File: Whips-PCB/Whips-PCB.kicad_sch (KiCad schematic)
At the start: 23 parts, among them J1 12 VDC, J2 RS422 BUS, J3 SPEAKER 4OHM, J4 TO WHIP, SW2 SW_DIP_x06, U2 MAX485ESA+T, U3 SN74AHCT125DR, U4 TSR_1-2450, U5 MAX98357AEWL_T, U6 Teensy4.1_Minimal

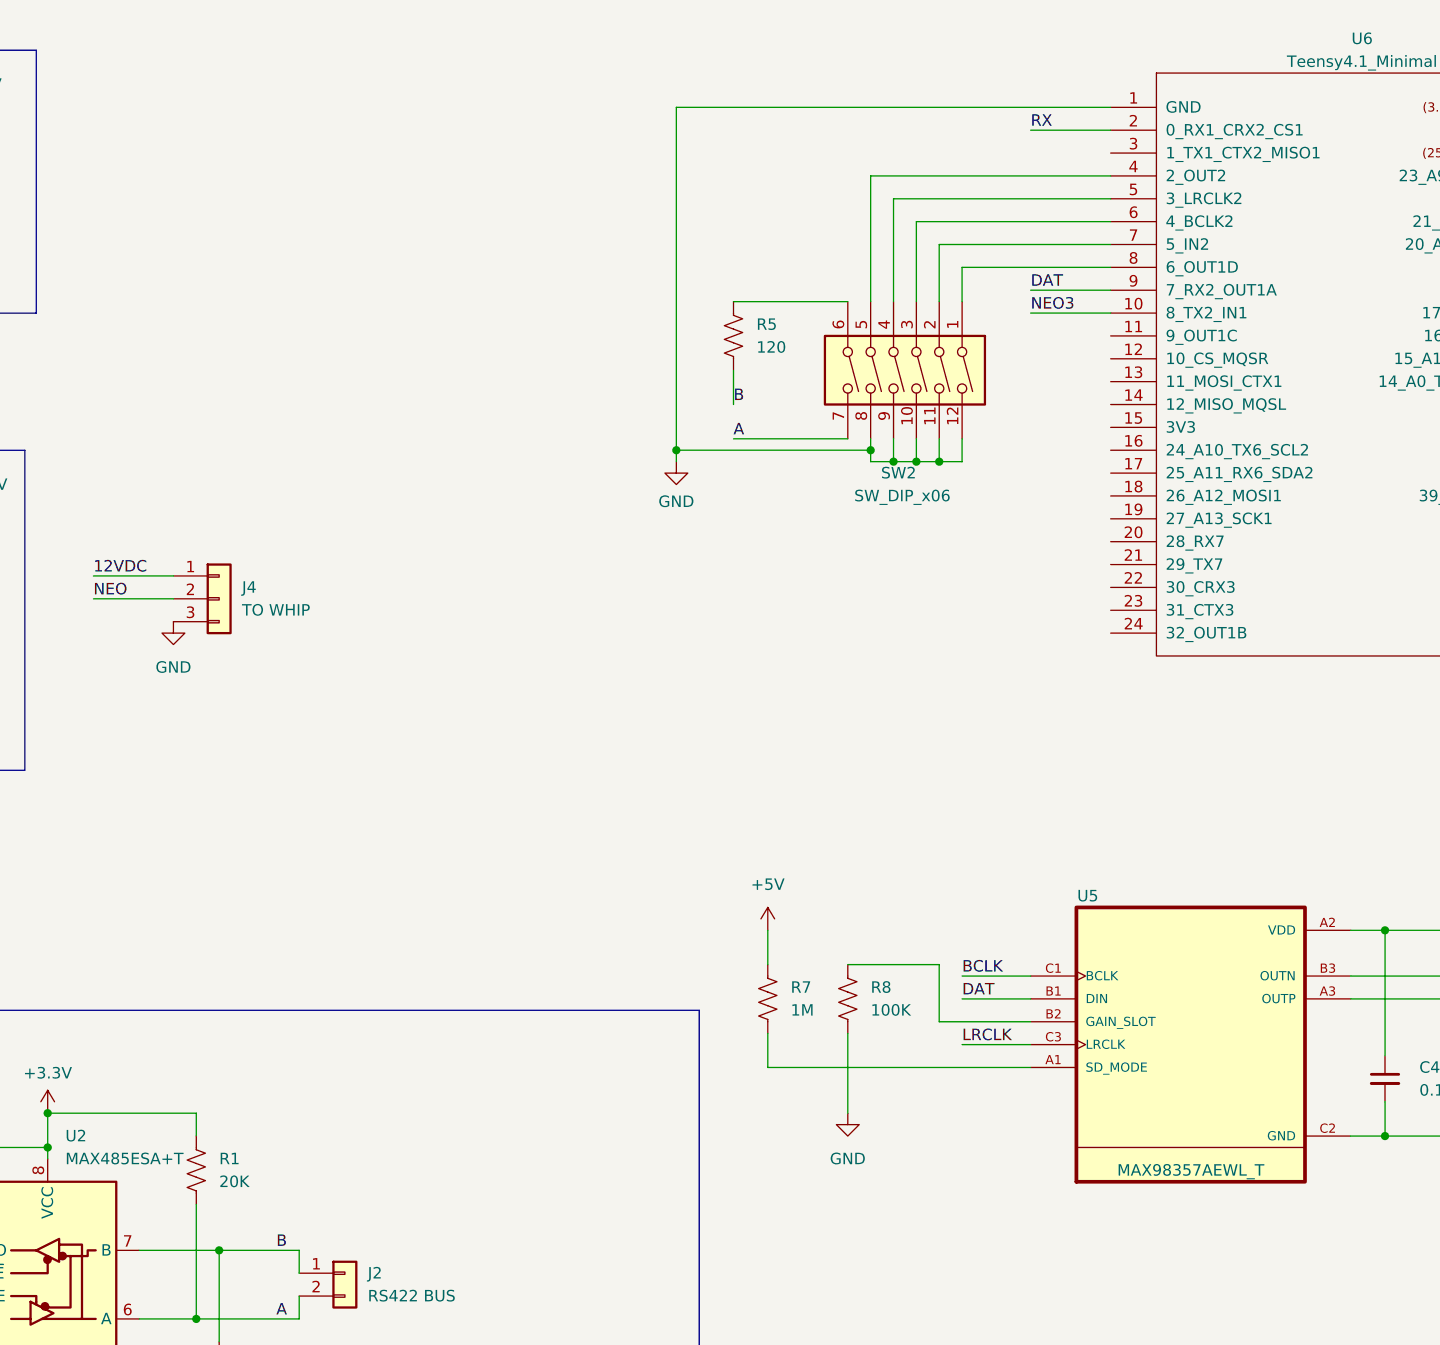
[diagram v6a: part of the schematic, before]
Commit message: support for indicator LEDS
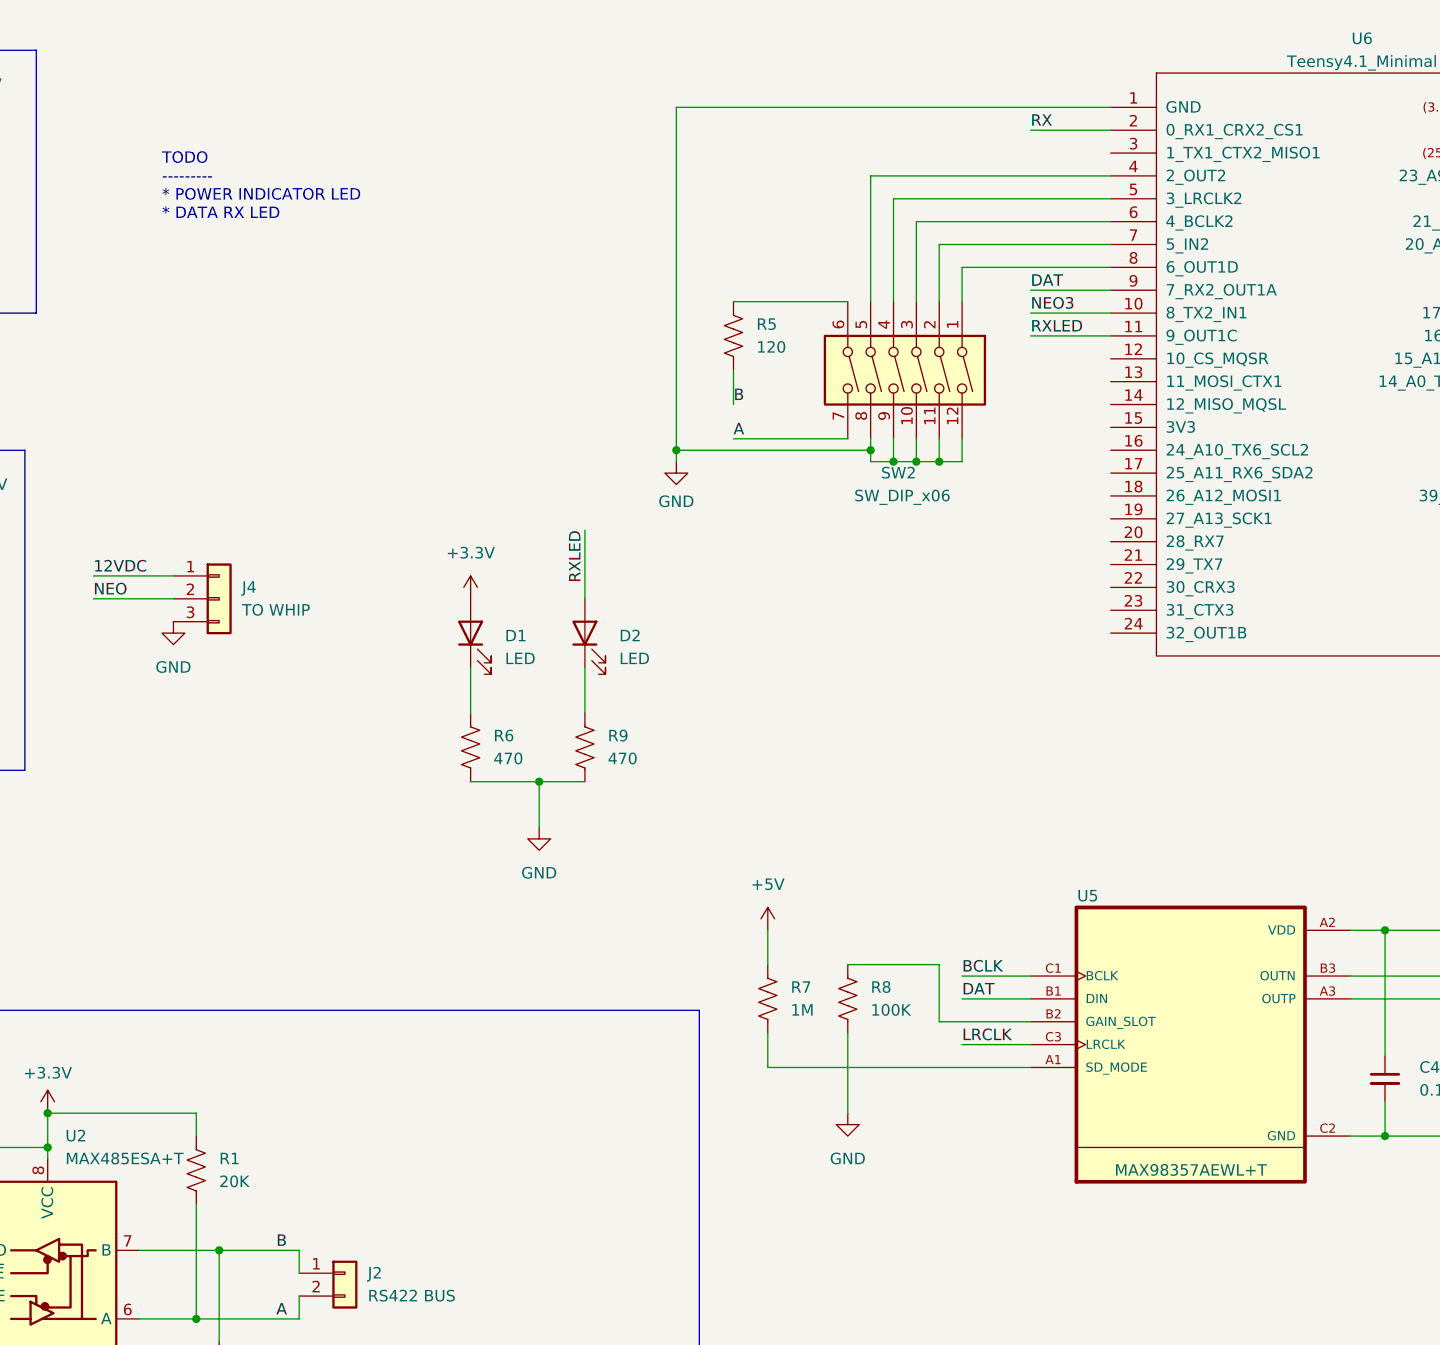
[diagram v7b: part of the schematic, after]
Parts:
- added D1, D2: LED, symbol Device:LED
- added R6, R9: 470, symbol Device:R_US
- C1, C4: footprint Capacitor_SMD:C_0201_0603Metric -> Capacitor_SMD:C_0402_1005Metric; LCSC C76934 -> C1525
- C2, C5: footprint Capacitor_SMD:C_0603_1608Metric -> Capacitor_SMD:C_0402_1005Metric; LCSC C1691 -> C15525
- J1, J2, J3: footprint (none) -> TerminalBlock_RND:TerminalBlock_RND_205-00001_1x02_P5.00mm_Horizontal; LCSC (none) -> C8404
- J4: footprint (none) -> TerminalBlock_RND:TerminalBlock_RND_205-00002_1x03_P5.00mm_Horizontal; LCSC (none) -> C8401
- R8: footprint Resistor_SMD:R_0805_2012Metric -> Resistor_SMD:R_0402_1005Metric; LCSC C149504 -> C25741
- SW2: footprint (none) -> Button_Switch_THT:SW_DIP_SPSTx06_Slide_6.7x16.8mm_W7.62mm_P2.54mm_LowProfile; LCSC C5160843 -> C2859410
- U2: footprint Package_SO:SOIC-8-1EP_3.9x4.9mm_P1.27mm_EP2.29x3mm -> Package_SO:SOIC-8_3.9x4.9mm_P1.27mm
- U4: LCSC (none) -> DNP
- U5: value MAX98357AEWL_T -> MAX98357AEWL+T; footprint MAX98357AEWL_T:BGA9N40P3X3_134X143X69N -> Package_BGA:WLP-9_1.448x1.468mm_Layout3x3_P0.4mm_Ball0.27mm_Pad0.25mm; LCSC (none) -> C2682619
- U6: footprint (none) -> teensy:Teensy41; LCSC (none) -> DNP
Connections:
- net +3.3V: now also D1.2 (A)
- net GND: now also R6.2, R9.2
- net RXLED: now reaches U6.11 (9_OUT1C)
- net RXLED: now also D2.2 (A)
- new net: D1.1 (K), R6.1
- new net: D2.1 (K), R9.1
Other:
- note added: "TODO --------- * POWER INDICATOR LED * DATA RX LED"

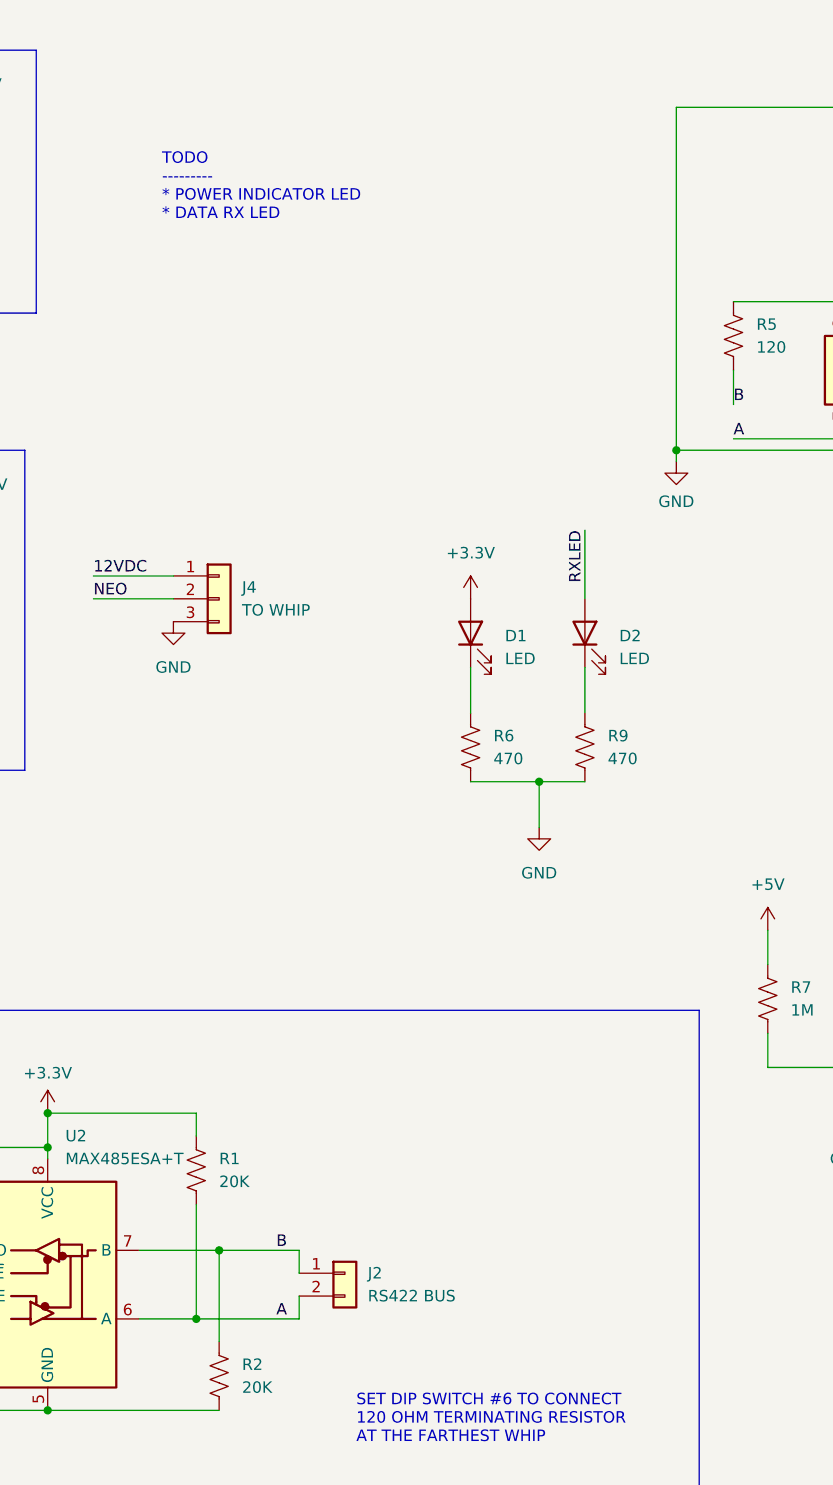
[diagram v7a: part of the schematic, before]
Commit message: provided parts and footprints for LEDs
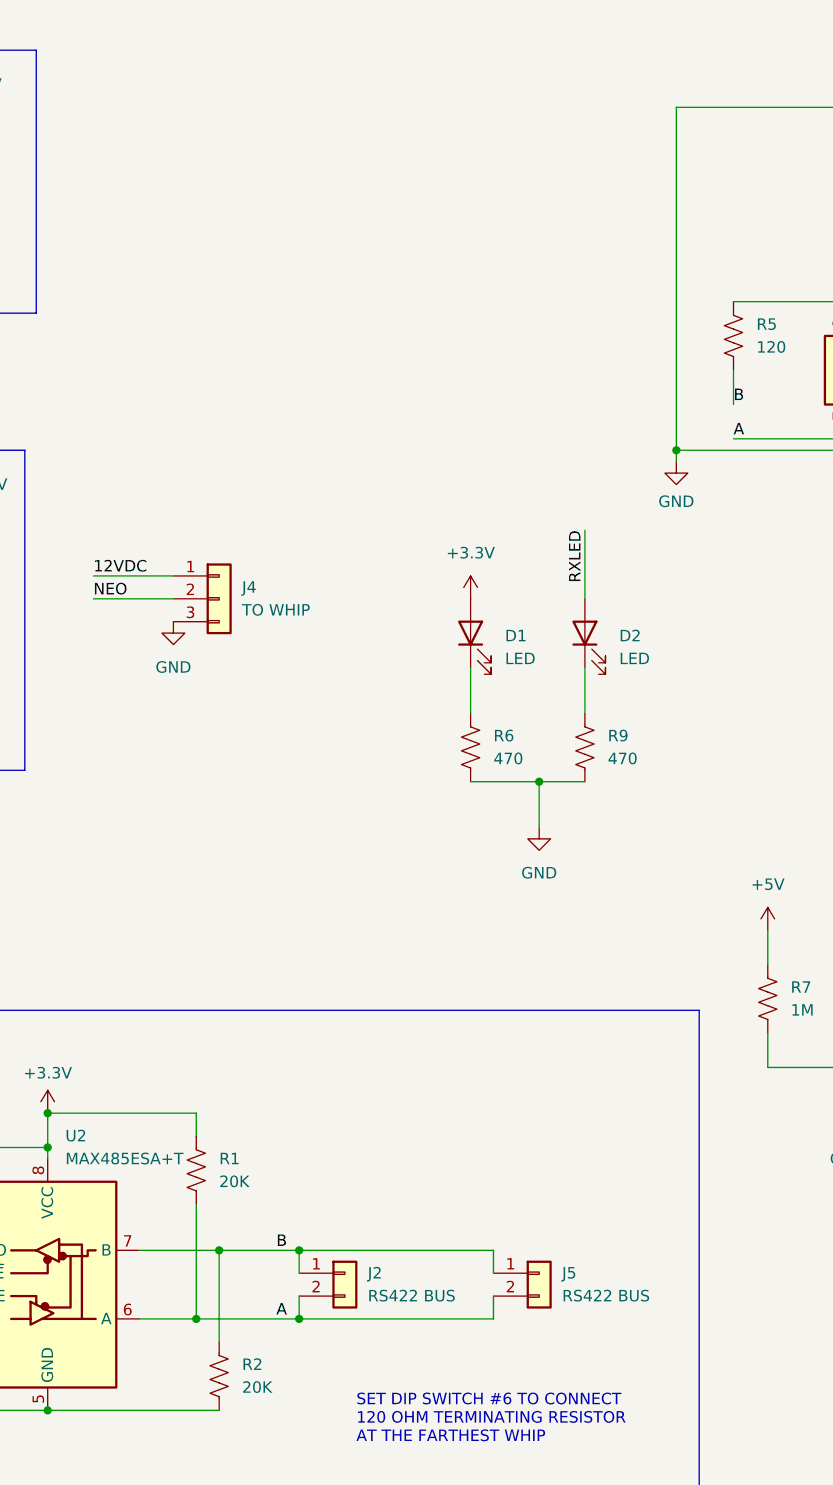
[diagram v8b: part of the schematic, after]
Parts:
- added J5: RS422 BUS, TerminalBlock_RND:TerminalBlock_RND_205-00001_1x02_P5.00mm_Horizontal, symbol Connector_Generic:Conn_01x02
- D1: footprint (none) -> LED_SMD:LED_0603_1608Metric; LCSC (none) -> C2286
- D2: footprint (none) -> LED_SMD:LED_0603_1608Metric; LCSC (none) -> C2290
- R6, R9: footprint (none) -> Resistor_SMD:R_0402_1005Metric; LCSC (none) -> C25117
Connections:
- net A: now also J5.2 (Pin_2)
- net B: now also J5.1 (Pin_1)
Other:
- note removed: "TODO --------- * POWER INDICATOR LED * DATA RX LED"
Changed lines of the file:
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@@
   (junction (at 212.09 123.19) (diameter 0) (color 0 0 0 0)
   )
+  (junction (at 91.44 166.37) (diameter 0) (color 0 0 0 0)
+  )
   (junction (at 223.52 123.19) (diameter 0) (color 0 0 0 0)
   )
@@
   )
   (junction (at 133.35 69.85) (diameter 0) (color 0 0 0 0)
+  )
+  (junction (at 91.44 158.75) (diameter 0) (color 0 0 0 0)
   )
   (junction (at 48.26 176.53) (diameter 0) (color 0 0 0 0)
@@
     (stroke (width 0) (type default))
   )
+  (wire (pts (xy 91.44 158.75) (xy 113.03 158.75))
+    (stroke (width 0) (type default))
+  )
   (wire (pts (xy 162.56 53.34) (xy 162.56 46.99))
     (stroke (width 0) (type default))
@@
     (stroke (width 0) (type default))
   )
+  (wire (pts (xy 113.03 158.75) (xy 113.03 161.29))
+    (stroke (width 0) (type default))
+  )
+  (wire (pts (xy 113.03 166.37) (xy 113.03 163.83))
+    (stroke (width 0) (type default))
+  )
   (wire (pts (xy 20.32 93.98) (xy 30.48 93.98))
     (stroke (width 0) (type default))
@@
     (stroke (width 0) (type default))
   )
+  (wire (pts (xy 91.44 166.37) (xy 113.03 166.37))
+    (stroke (width 0) (type default))
+  )
   (wire (pts (xy 251.46 34.29) (xy 237.49 34.29))
     (stroke (width 0) (type default))
@@
   )
   (text "NEOPIXEL LEVEL SHIFTER" (at 19.05 68.58 0)
-    (effects (font (size 1.27 1.27)) (justify left bottom))
-  )
-  (text "TODO\n---------\n* POWER INDICATOR LED\n* DATA RX LED"
-    (at 76.2 44.45 0)
     (effects (font (size 1.27 1.27)) (justify left bottom))
   )
@@
       (effects (font (size 1.27 1.27)) (justify right))
     )
-    (property "Footprint" "" (at 110.49 90.17 0)
+    (property "Footprint" "LED_SMD:LED_0603_1608Metric" (at 110.49 90.17 0)
       (effects (font (size 1.27 1.27)) hide)
     )
@@
       (effects (font (size 1.27 1.27)) hide)
     )
+    (property "LCSC" "C2286" (at 110.49 90.17 0)
+      (effects (font (size 1.27 1.27)) hide)
+    )
     (pin "1")
     (pin "2")
@@
       (effects (font (size 1.27 1.27)) (justify left))
     )
-    (property "Footprint" "" (at 111.506 103.124 90)
+    (property "Footprint" "Resistor_SMD:R_0402_1005Metric" (at 111.506 103.124 90)
       (effects (font (size 1.27 1.27)) hide)
     )
     (property "Datasheet" "~" (at 110.49 102.87 0)
+      (effects (font (size 1.27 1.27)) hide)
+    )
+    (property "LCSC" "C25117" (at 110.49 102.87 0)
       (effects (font (size 1.27 1.27)) hide)
     )
@@
       (effects (font (size 1.27 1.27)) (justify right))
     )
-    (property "Footprint" "" (at 123.19 90.17 0)
+    (property "Footprint" "LED_SMD:LED_0603_1608Metric" (at 123.19 90.17 0)
       (effects (font (size 1.27 1.27)) hide)
     )
@@
       (effects (font (size 1.27 1.27)) hide)
     )
+    (property "LCSC" "C2290" (at 123.19 90.17 0)
+      (effects (font (size 1.27 1.27)) hide)
+    )
     (pin "1")
     (pin "2")
@@
       (effects (font (size 1.27 1.27)) (justify left))
     )
-    (property "Footprint" "" (at 124.206 103.124 90)
+    (property "Footprint" "Resistor_SMD:R_0402_1005Metric" (at 124.206 103.124 90)
       (effects (font (size 1.27 1.27)) hide)
     )
@@
       (effects (font (size 1.27 1.27)) hide)
     )
+    (property "LCSC" "C25117" (at 123.19 102.87 0)
+      (effects (font (size 1.27 1.27)) hide)
+    )
     (pin "1")
     (pin "2")
@@
         )
       )
+    )
+  )
+  (symbol (lib_id "Connector_Generic:Conn_01x02") (at 118.11 161.29 0) (unit 1)
+    (in_bom yes) (on_board yes) (dnp no) (fields_autoplaced)
+    (property "Reference" "J5" (at 120.65 161.29 0)
+      (effects (font (size 1.27 1.27)) (justify left))
+    )
+    (property "Value" "RS422 BUS" (at 120.65 163.83 0)
+      (effects (font (size 1.27 1.27)) (justify left))
+    )
+    (property "Footprint" "TerminalBlock_RND:TerminalBlock_RND_205-00001_1x02_P5.00mm_Horizontal" (at 118.11 161.29 0)
+      (effects (font (size 1.27 1.27)) hide)
+    )
+    (property "Datasheet" "~" (at 118.11 161.29 0)
+      (effects (font (size 1.27 1.27)) hide)
+    )
+    (property "LCSC" "C8404" (at 118.11 161.29 0)
+      (effects (font (size 1.27 1.27)) hide)
+    )
+    (pin "1")
+    (pin "2")
+    (instances
+      (project "Whips-PCB"
+        (path "/f51f4695-2f3c-4442-ab83-4885bbbb2720"
+          (reference "J5") (unit 1)
+        )
+      )
